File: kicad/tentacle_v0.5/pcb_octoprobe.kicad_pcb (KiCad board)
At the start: 2 copper layers, 100 x 165 mm, 737 parts, among them J1302 Conn_02x20, J1303 Conn_02x20, J1501 Conn_02x20, J1502 Conn_01x12, J201 Conn_02x05, J202 Conn_01x5, J301 USB_C_Receptacle_USB2.0, J501 Conn_02x20, U1001 GAQY221S, U1101 GAQY221S, U1201 GAQY221S, U1501 RP2040, U1502 W25Q32JVS, U1503 TXB0108PW, U201 RP2040, U202 AMS1117-3.3, U203 W25Q32JVS, U204 TPS2595xx, U205 TPS2595xx, U206 MT9700, U302 USB2514B_Bi, U601 GAQY221S, U701 GAQY221S, U801 GAQY221S, U901 GAQY221S, X201 Oscillator-12MHz, Y301 24MHz

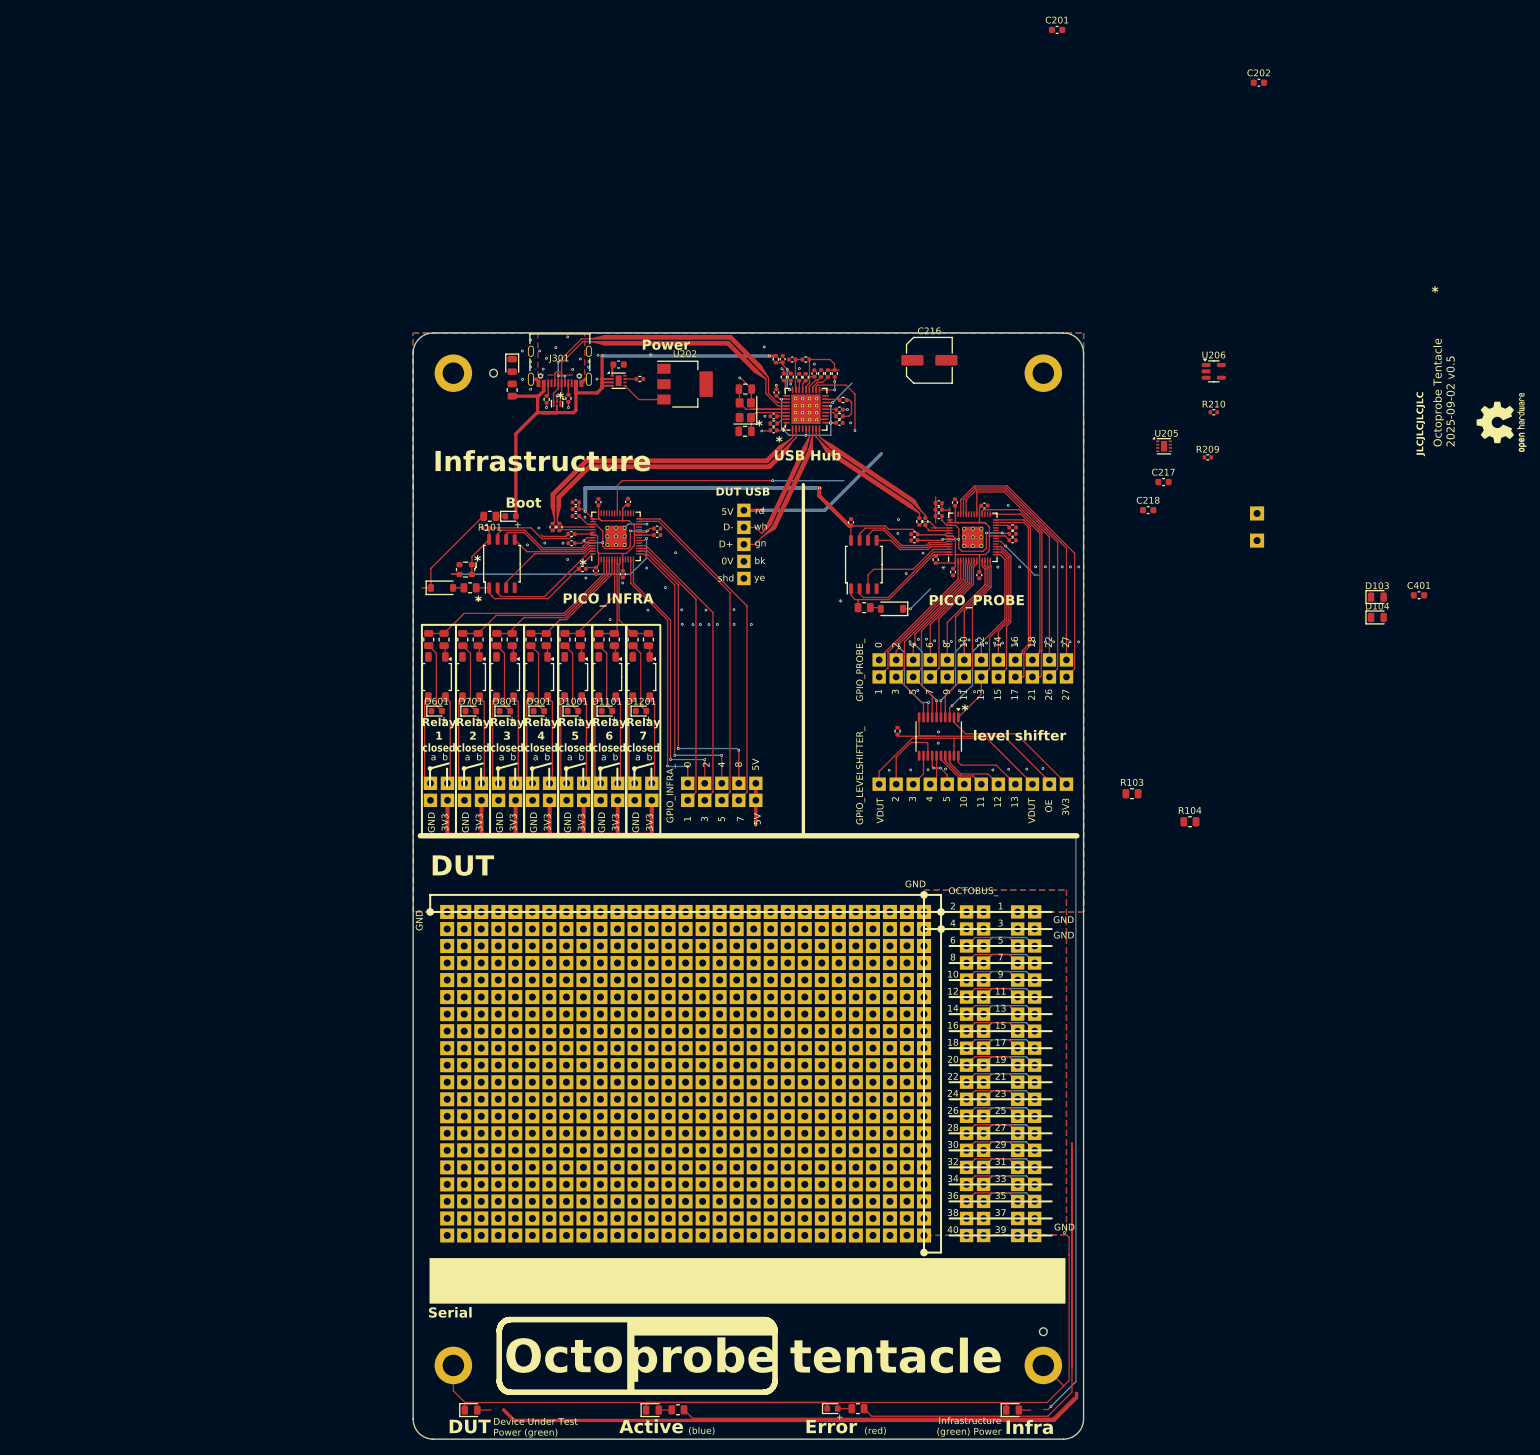
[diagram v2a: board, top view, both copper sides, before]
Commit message: ERC and DRC without errors and warnings LEDS less bright (Green LEDs 2k2 -> 4k7)
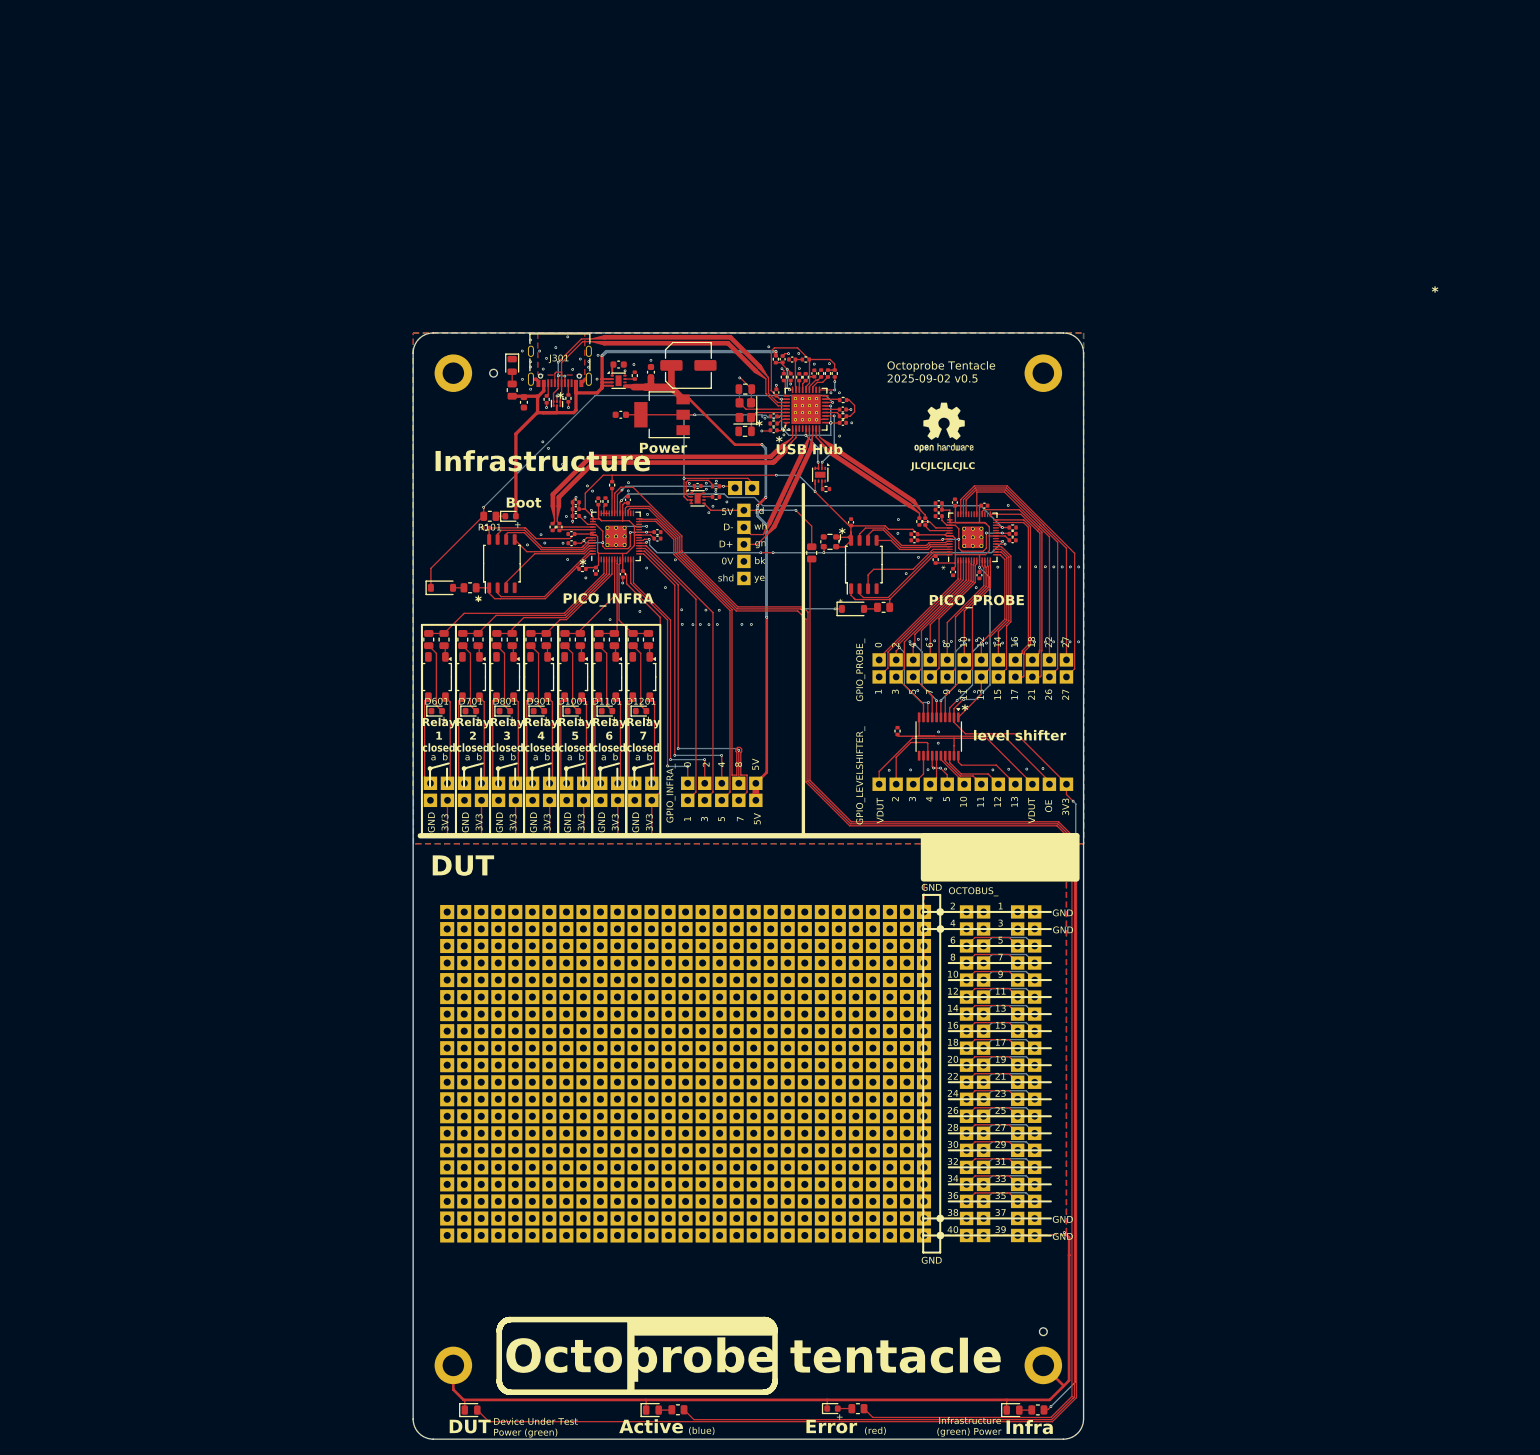
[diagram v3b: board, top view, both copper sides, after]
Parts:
- removed the ? at (127.3, 103.6)
- removed the ? at (63.8, 103.6)
- removed the ? at (112.1, 103.6)
- removed the ? at (117.2, 103.6)
- removed the ? at (122.3, 103.6)
- removed the ? at (66.4, 103.6)
- removed the ? at (94.3, 103.6)
- removed the ? at (91.8, 103.6)
- removed the ? at (132.4, 103.6)
- removed the ? at (71.5, 103.6)
- removed the ? at (84.2, 103.6)
- removed the ? at (119.7, 103.6)
- removed the ? at (104.5, 103.6)
- removed the ? at (101.9, 103.6)
- removed the ? at (68.9, 103.6)
- removed the ? at (89.2, 103.6)
- removed the ? at (96.9, 103.6)
- removed the ? at (81.6, 103.6)
- removed the ? at (76.5, 103.6)
- removed the ? at (129.9, 103.6)
- removed the ? at (114.6, 103.6)
- removed the ? at (79.1, 103.6)
- removed the ? at (109.6, 103.6)
- removed the ? at (99.4, 103.6)
- removed the ? at (86.7, 103.6)
- removed the ? at (124.8, 103.6)
- removed the ? at (107.0, 103.6)
- removed the ? at (74.0, 103.6)
- removed C218: 10u, Capacitor_SMD:C_0603_1608Metric
- removed the D103 at (67.4, 177.9)
- removed the D104 at (148.2, 177.9)
- removed U206: MT9700, Package_TO_SOT_SMD:SOT-23-5
- added ?: prototype_NC, 00_project_library:octoprobe_breakout_PB_NC, F.Cu at (132.4, 103.6)
- added ?: prototype_NC, 00_project_library:octoprobe_breakout_PB_NC, F.Cu at (114.6, 103.6)
- added ?: prototype_NC, 00_project_library:octoprobe_breakout_PB_NC, F.Cu at (124.8, 103.6)
- added ?: prototype_NC, 00_project_library:octoprobe_breakout_PB_NC, F.Cu at (91.8, 103.6)
- added ?: prototype_NC, 00_project_library:octoprobe_breakout_PB_NC, F.Cu at (127.3, 103.6)
- added ?: prototype_NC, 00_project_library:octoprobe_breakout_PB_NC, F.Cu at (129.9, 103.6)
- added ?: prototype_NC, 00_project_library:octoprobe_breakout_PB_NC, F.Cu at (63.8, 103.6)
- added ?: prototype_NC, 00_project_library:octoprobe_breakout_PB_NC, F.Cu at (122.3, 103.6)
- added ?: prototype_NC, 00_project_library:octoprobe_breakout_PB_NC, F.Cu at (84.2, 103.6)
- added ?: prototype_NC, 00_project_library:octoprobe_breakout_PB_NC, F.Cu at (104.5, 103.6)
- added ?: prototype_NC, 00_project_library:octoprobe_breakout_PB_NC, F.Cu at (86.7, 103.6)
- added ?: prototype_NC, 00_project_library:octoprobe_breakout_PB_NC, F.Cu at (109.6, 103.6)
- added ?: prototype_NC, 00_project_library:octoprobe_breakout_PB_NC, F.Cu at (68.9, 103.6)
- added ?: prototype_NC, 00_project_library:octoprobe_breakout_PB_NC, F.Cu at (112.1, 103.6)
- added ?: prototype_NC, 00_project_library:octoprobe_breakout_PB_NC, F.Cu at (66.4, 103.6)
- added ?: prototype_NC, 00_project_library:octoprobe_breakout_PB_NC, F.Cu at (96.9, 103.6)
- added ?: prototype_NC, 00_project_library:octoprobe_breakout_PB_NC, F.Cu at (107.0, 103.6)
- added ?: prototype_NC, 00_project_library:octoprobe_breakout_PB_NC, F.Cu at (81.6, 103.6)
- added ?: prototype_NC, 00_project_library:octoprobe_breakout_PB_NC, F.Cu at (101.9, 103.6)
- added ?: prototype_NC, 00_project_library:octoprobe_breakout_PB_NC, F.Cu at (94.3, 103.6)
- added ?: prototype_NC, 00_project_library:octoprobe_breakout_PB_NC, F.Cu at (71.5, 103.6)
- added ?: prototype_NC, 00_project_library:octoprobe_breakout_PB_NC, F.Cu at (79.1, 103.6)
- added ?: prototype_NC, 00_project_library:octoprobe_breakout_PB_NC, F.Cu at (89.2, 103.6)
- added ?: prototype_NC, 00_project_library:octoprobe_breakout_PB_NC, F.Cu at (76.5, 103.6)
- added ?: prototype_NC, 00_project_library:octoprobe_breakout_PB_NC, F.Cu at (99.4, 103.6)
- added ?: prototype_NC, 00_project_library:octoprobe_breakout_PB_NC, F.Cu at (74.0, 103.6)
- added ?: prototype_NC, 00_project_library:octoprobe_breakout_PB_NC, F.Cu at (119.7, 103.6)
- added ?: prototype_NC, 00_project_library:octoprobe_breakout_PB_NC, F.Cu at (117.2, 103.6)
- added R211: 100k, Resistor_SMD:R_0402_1005Metric, F.Cu at (103.9, 40.1)
- added R212: 33K, Resistor_SMD:R_0402_1005Metric, F.Cu at (120.3, 40.5)
- added R213: 10K, Resistor_SMD:R_0402_1005Metric, F.Cu at (88.4, 40.0)
- added U207: TPS2595xx, Package_SON:WSON-8-1EP_2x2mm_P0.5mm_EP0.9x1.6mm, F.Cu at (119.5, 38.4)
- C217: value 10u -> 1u; footprint Capacitor_SMD:C_0603_1608Metric -> Capacitor_SMD:C_0402_1005Metric
- R210: value 12k -> 10K
- moved D103 181.6 mm to (67.4, 177.9)
- moved C401 136.6 mm to (75.3, 27.6), turned to 90 degrees
- moved D104 130.1 mm to (148.2, 177.9)
- moved C202 107.3 mm to (89.7, 29.5), turned to 180 degrees
- moved R210 91.7 mm to (87.5, 42.4), turned to 90 degrees
- moved R104 90.6 mm to (151.9, 177.9)
- moved Logo_open_hardware101 83.2 mm to (137.9, 31.4), turned to 0 degrees
- moved C201 79.2 mm to (94.2, 23.1), turned to 90 degrees
- moved BP201 78.0 mm to (106.8, 40.4)
- moved BP202 75.7 mm to (109.3, 40.4)
- moved R209 73.6 mm to (103.9, 41.7), turned to 180 degrees
- moved U205 70.0 mm to (101.2, 41.9)
- moved C217 69.5 mm to (101.2, 40.1)
- moved R103 59.8 mm to (118.2, 50.1), turned to 90 degrees
- moved X201 54.5 mm to (120.9, 48.4)
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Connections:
- BP201 pad 1: +3V3dut -> DUT_PWR_EN
- R210 pad 1: GND -> Net-(U201-GPIO26/ADC0)
- R210 pad 2: Net-(U206-SET) -> GND
- U201 pad 37: unconnected-(U201-GPIO25-Pad37) -> Net-(U201-GPIO25)
- U201 pad 38: unconnected-(U201-GPIO26/ADC0-Pad38) -> Net-(U201-GPIO26/ADC0)
- U201 pad 39: unconnected-(U201-GPIO27/ADC1-Pad39) -> Net-(U201-GPIO26/ADC0)
- U201 pad 40: unconnected-(U201-GPIO28/ADC2-Pad40) -> Net-(U201-GPIO26/ADC0)
- U201 pad 41: unconnected-(U201-GPIO29/ADC3-Pad41) -> Net-(U201-GPIO26/ADC0)
- U205 pad 2: DUT_PWR_EN -> Net-(U205-EN/UVLO)
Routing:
- net Net-(D103-A): track 2.04 -> 251.3 mm
- net +3V3infra: track 257.9 -> 420.5 mm, vias 2 -> 6
- net Net-(U201-GPIO20): track 103.6 -> 218.6 mm
- net Net-(U201-GPIO24): track 148.2 -> 253.2 mm
- net (no net): track 87.9 -> 0.00 mm, vias 1 -> 4
- net +5Vbuf: track 12.9 -> 88.4 mm, vias 1 -> 4
- net +3V3: track 41.5 -> 111.1 mm, vias 5 -> 8
- net RP2_PROBE_RUN: track 2.14 -> 63.5 mm, vias 0 -> 2
- net RP2_INFRA_BOOT: track 20.6 -> 75.9 mm, vias 1 -> 2
- net RP2_PROBE_BOOT: track 5.36 -> 41.1 mm, vias 1 -> 2
- net GND: track 182.3 -> 159.5 mm, vias 103 -> 133
- net DUT_PWR_EN: track 38.2 -> 21.5 mm, vias 1 -> 2
- net /RP2 CPU/12MHz: track 43.9 -> 58.2 mm, vias 2 -> 5
- net /USB Hub Chip/PRT_PWR4: track 12.4 -> 0.00 mm, vias 1 -> 0
- net RP2_INFRA_PWR_EN: track 0.00 -> 9.96 mm, vias 0 -> 2
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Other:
- board text removed: "DUT USB"
- board text removed: "Serial"
